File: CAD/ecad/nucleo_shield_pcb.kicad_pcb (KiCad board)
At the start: 2 copper layers, 70 x 57 mm, 19 parts, among them J1 Conn_02x19_Odd_Even, J2 CN10, J3 Conn_01x02_Pin, J4 Conn_01x04_Socket, J5 Conn_01x03_Pin, J6 Conn_01x06_Pin, SW1 CK_KMS2xxGP, SW2 CK_KMS2xxGP, SW3 CK_KMS2xxGP, U1 ESP32-CAM, U2 ADXL345, U3 HC-SR04, U4 DM-OLED096-636

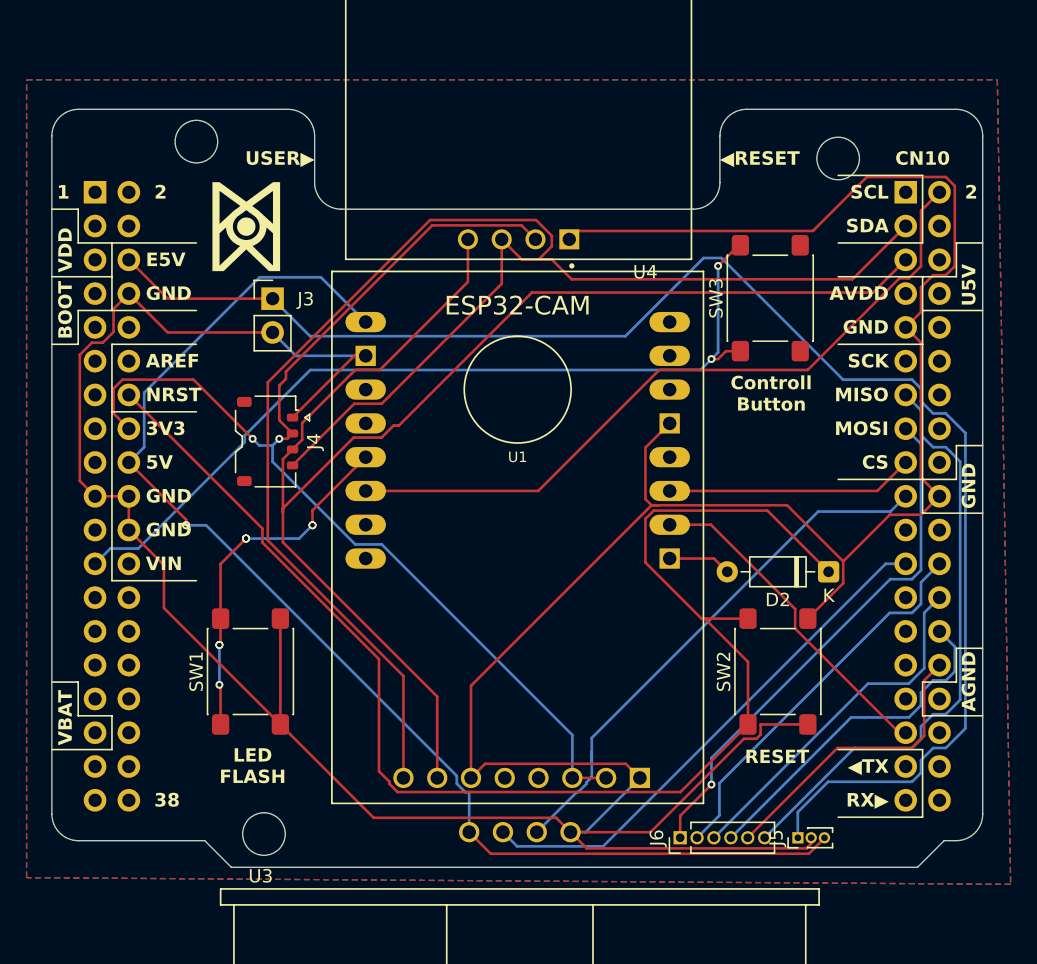
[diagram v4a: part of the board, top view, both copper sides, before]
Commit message: Configure 2.0mm JST PH connector for SGP30 sensor and generate Gerbers
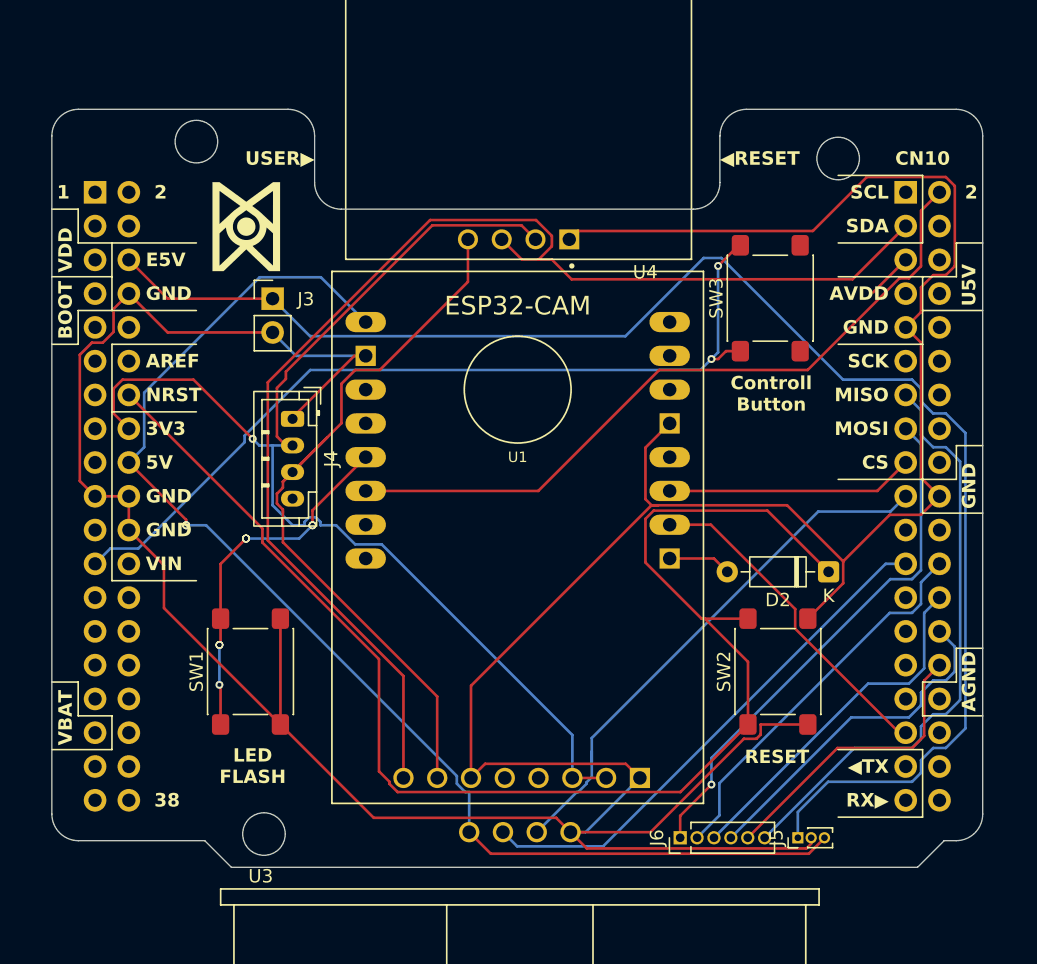
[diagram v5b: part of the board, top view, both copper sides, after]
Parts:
- J4: footprint Connector_JST:JST_ACH_BM04B-ACHSS-A-GAN-ETF_1x04-1MP_P1.20mm_Vertical -> Connector_JST:JST_PH_B4B-PH-K_1x04_P2.00mm_Vertical
- moved J4 2.53 mm to (135.5, 78.0)
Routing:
- net /SDA: track 107.1 -> 61.7 mm
- net /SCL: track 121.1 -> 96.4 mm
- net +3V3: track 86.7 -> 90.4 mm, vias 2 -> 1
- removed copper zone on B.Cu, net GNDD
- removed copper zone on F.Cu, net GNDD
